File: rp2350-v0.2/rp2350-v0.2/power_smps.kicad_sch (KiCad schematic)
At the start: 23 parts, among them IC3 BQ25628ERYKR

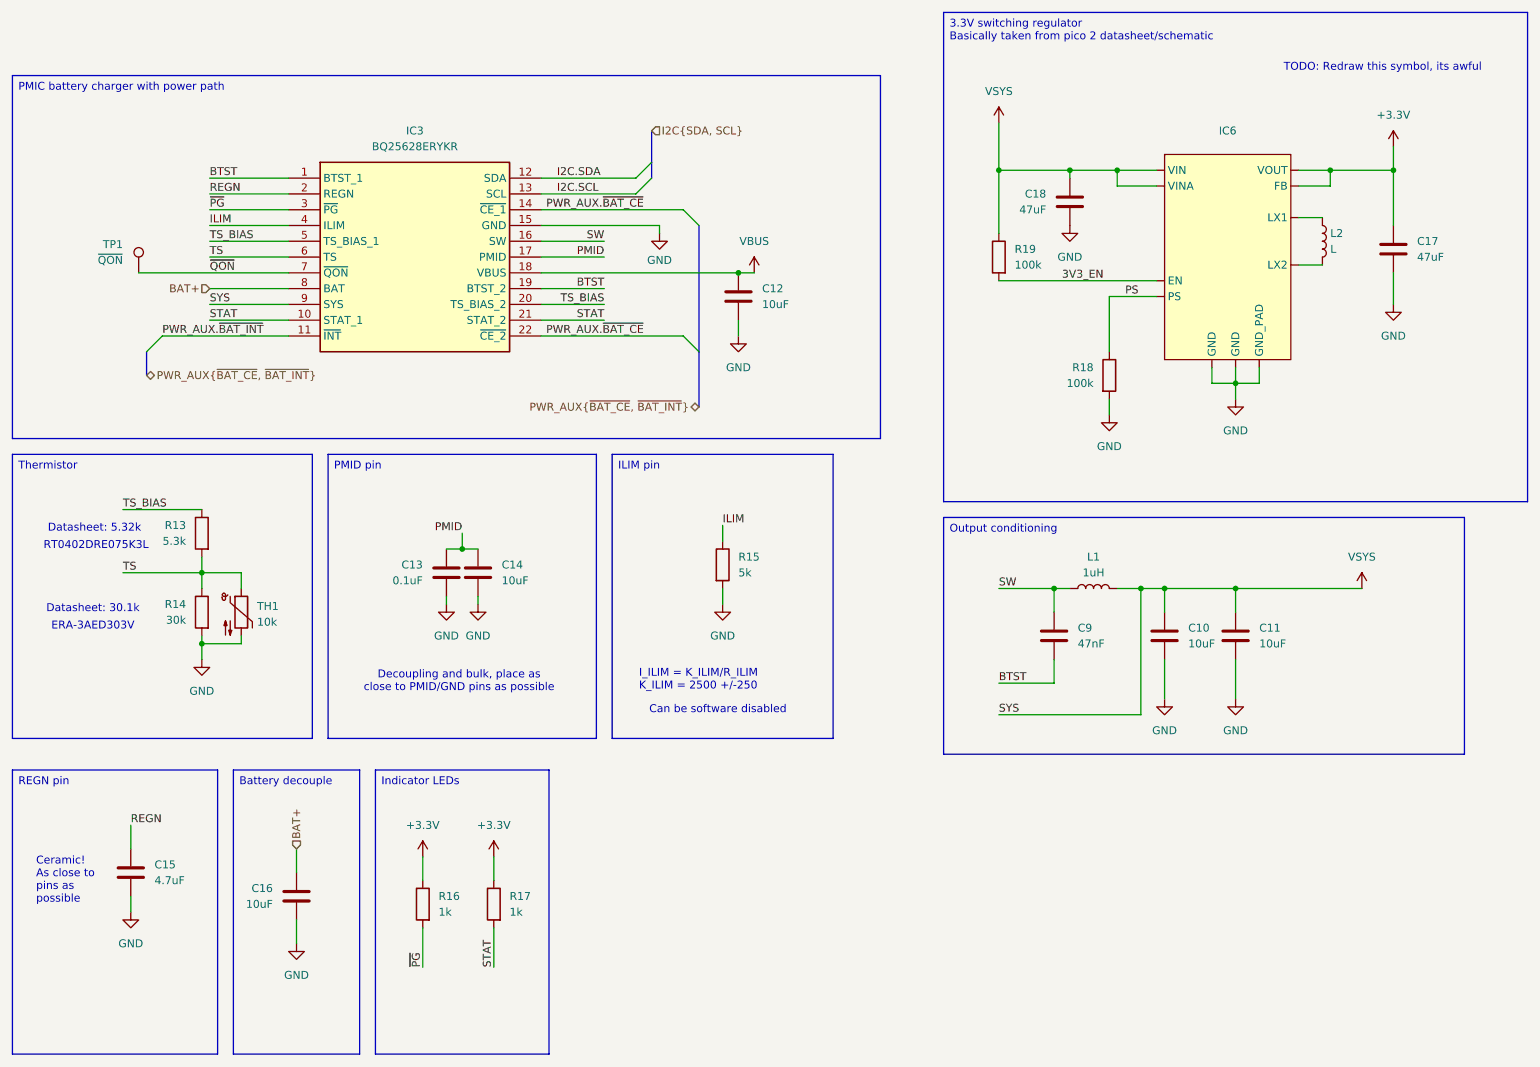
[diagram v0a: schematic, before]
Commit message: v0.2: schematic draft 1 done
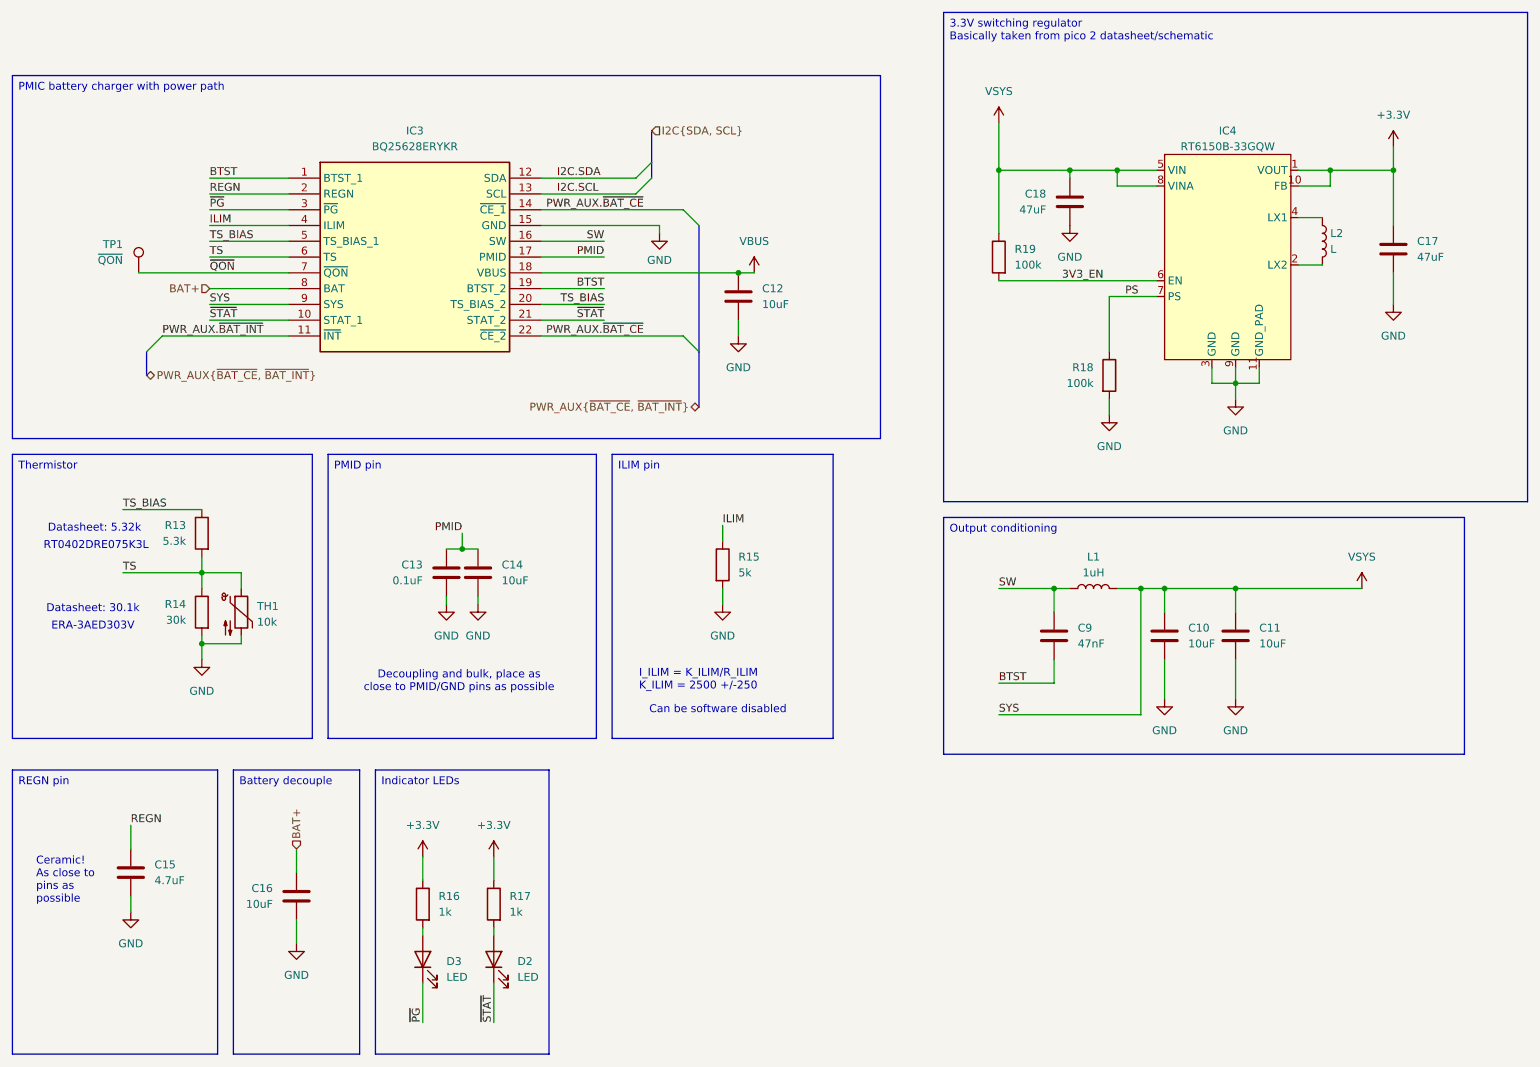
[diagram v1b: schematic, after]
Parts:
- removed IC6: ~, SamacSys_Parts:SON50P250X250X80-11N-D, symbol SamacSys_Parts:RT6150B-33GQW-Custom
- added D2, D3: LED, LED_SMD:LED_0402_1005Metric, symbol Device:LED
- added IC4: RT6150B-33GQW, SamacSys_Parts:SON50P250X250X80-11N-D, symbol CustomSymbols:RT6150B-33GQW
- TP1: footprint (none) -> TestPoint:TestPoint_Pad_2.5x2.5mm
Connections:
- net +3.3V: now also IC4.1 (VOUT), IC4.10 (FB)
- net 3V3_EN: now also IC4.6 (EN)
- net GND: now also IC4.11 (GND_PAD), IC4.3 (GND), IC4.9 (GND)
- net PS: now also IC4.7 (PS)
- net VSYS: now also IC4.5 (VIN), IC4.8 (VINA)
- net ~{PG}: now also D3.1 (K); no longer R16.2
- net at L2.1: now also IC4.4 (LX1)
- net at L2.2: now also IC4.2 (LX2)
- net STAT renamed ~{STAT}
- net ~{STAT}: now also D2.1 (K); no longer R17.2
- new net: D2.2 (A), R17.2
- new net: D3.2 (A), R16.2
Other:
- note removed: "TODO: Redraw this symbol, its awful"
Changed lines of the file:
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@@
 		)
 	)
-	(text "TODO: Redraw this symbol, its awful"
-		(exclude_from_sim no)
-		(at 259.334 25.4 0)
-		(effects
-			(font
-				(size 1.27 1.27)
-			)
-			(justify right)
-		)
-	)
 	(text_box "3.3V switching regulator\nBasically taken from pico 2 datasheet/schematic"
 		(exclude_from_sim no)
@@
 	(wire
 		(pts
-			(xy 88.9 163.83) (xy 88.9 170.18)
+			(xy 88.9 163.83) (xy 88.9 165.1)
 		)
 		(stroke
@@
 	(wire
 		(pts
-			(xy 100.33 163.83) (xy 100.33 170.18)
+			(xy 100.33 163.83) (xy 100.33 165.1)
 		)
 		(stroke
@@
 	(wire
 		(pts
+			(xy 88.9 172.72) (xy 88.9 179.07)
+		)
+		(stroke
+			(width 0)
+			(type default)
+		)
+	)
+	(wire
+		(pts
 			(xy 234.95 41.91) (xy 245.11 41.91)
 		)
@@
 	(wire
 		(pts
+			(xy 100.33 172.72) (xy 100.33 179.07)
+		)
+		(stroke
+			(width 0)
+			(type default)
+		)
+	)
+	(wire
+		(pts
 			(xy 107.95 63.5) (xy 118.11 63.5)
 		)
@@
 		)
 	)
-	(label "STAT"
+	(label "~{STAT}"
 		(at 54.61 66.04 0)
 		(effects
@@
 	)
 	(label "~{PG}"
-		(at 88.9 170.18 90)
+		(at 88.9 179.07 90)
 		(effects
 			(font
@@
 		)
 	)
-	(label "STAT"
+	(label "~{STAT}"
 		(at 118.11 66.04 180)
 		(effects
@@
 		)
 	)
-	(label "STAT"
-		(at 100.33 170.18 90)
+	(label "~{STAT}"
+		(at 100.33 179.07 90)
 		(effects
 			(font
@@
 			)
 		)
-		(property "Footprint" ""
+		(property "Footprint" "TestPoint:TestPoint_Pad_2.5x2.5mm"
 			(at 48.26 58.42 0)
 			(effects
@@
 	)
 	(symbol
-		(lib_id "SamacSys_Parts:RT6150B-33GQW-Custom")
-		(at 218.44 38.1 0)
-		(unit 1)
-		(exclude_from_sim no)
-		(in_bom yes)
-		(on_board yes)
-		(dnp no)
-		(fields_autoplaced yes)
-		(property "Reference" "IC6"
-			(at 218.44 35.56 0)
-			(effects
-				(font
-					(size 1.27 1.27)
-				)
-			)
-		)
-		(property "Value" "~"
-			(at 218.44 38.1 0)
-			(effects
-				(font
-					(size 1.27 1.27)
-				)
-			)
-		)
-		(property "Footprint" "SamacSys_Parts:SON50P250X250X80-11N-D"
-			(at 218.44 38.1 0)
-			(effects
-				(font
-					(size 1.27 1.27)
-				)
-				(hide yes)
-			)
-		)
-		(property "Datasheet" ""
-			(at 218.44 38.1 0)
-			(effects
-				(font
-					(size 1.27 1.27)
-				)
-				(hide yes)
-			)
-		)
-		(property "Description" ""
-			(at 218.44 38.1 0)
-			(effects
-				(font
-					(size 1.27 1.27)
-				)
-				(hide yes)
-			)
-		)
-		(pin ""
-		)
-		(pin ""
-		)
-		(pin ""
-		)
-		(pin ""
-		)
-		(pin ""
-		)
-		(pin ""
-		)
-		(pin ""
-		)
-		(pin ""
-		)
-		(pin ""
-		)
-		(pin ""
-		)
-		(pin ""
-		)
-		(instances
-			(project ""
-				(path "/5cbb45d4-7f83-48dd-a53b-5c75c7d1d827/e9800bf9-b30f-4ca1-94ae-2aa68cc9dec4"
-					(reference "IC6")
-					(unit 1)
-				)
-			)
-		)
-	)
-	(symbol
 		(lib_id "power:GND")
 		(at 68.58 166.37 0)
@@
 	)
 	(symbol
+		(lib_id "Device:LED")
+		(at 100.33 168.91 90)
+		(unit 1)
+		(exclude_from_sim no)
+		(in_bom yes)
+		(on_board yes)
+		(dnp no)
+		(fields_autoplaced yes)
+		(property "Reference" "D2"
+			(at 104.14 169.2274 90)
+			(effects
+				(font
+					(size 1.27 1.27)
+				)
+				(justify right)
+			)
+		)
+		(property "Value" "LED"
+			(at 104.14 171.7674 90)
+			(effects
+				(font
+					(size 1.27 1.27)
+				)
+				(justify right)
+			)
+		)
+		(property "Footprint" "LED_SMD:LED_0402_1005Metric"
+			(at 100.33 168.91 0)
+			(effects
+				(font
+					(size 1.27 1.27)
+				)
+				(hide yes)
+			)
+		)
+		(property "Datasheet" "~"
+			(at 100.33 168.91 0)
+			(effects
+				(font
+					(size 1.27 1.27)
+				)
+				(hide yes)
+			)
+		)
+		(property "Description" "Light emitting diode"
+			(at 100.33 168.91 0)
+			(effects
+				(font
+					(size 1.27 1.27)
+				)
+				(hide yes)
+			)
+		)
+		(property "Sim.Pins" "1=K 2=A"
+			(at 100.33 168.91 0)
+			(effects
+				(font
+					(size 1.27 1.27)
+				)
+				(hide yes)
+			)
+		)
+		(pin "2"
+		)
+		(pin "1"
+		)
+		(instances
+			(project ""
+				(path "/5cbb45d4-7f83-48dd-a53b-5c75c7d1d827/e9800bf9-b30f-4ca1-94ae-2aa68cc9dec4"
+					(reference "D2")
+					(unit 1)
+				)
+			)
+		)
+	)
+	(symbol
 		(lib_id "Device:C")
 		(at 97.79 106.68 0)
@@
 	)
 	(symbol
+		(lib_id "CustomSymbols:RT6150B-33GQW")
+		(at 218.44 38.1 0)
+		(unit 1)
+		(exclude_from_sim no)
+		(in_bom yes)
+		(on_board yes)
+		(dnp no)
+		(fields_autoplaced yes)
+		(property "Reference" "IC4"
+			(at 218.44 35.56 0)
+			(effects
+				(font
+					(size 1.27 1.27)
+				)
+			)
+		)
+		(property "Value" "RT6150B-33GQW"
+			(at 218.44 38.1 0)
+			(effects
+				(font
+					(size 1.27 1.27)
+				)
+			)
+		)
+		(property "Footprint" "SamacSys_Parts:SON50P250X250X80-11N-D"
+			(at 218.44 38.1 0)
+			(effects
+				(font
+					(size 1.27 1.27)
+				)
+				(hide yes)
+			)
+		)
+		(property "Datasheet" ""
+			(at 218.44 38.1 0)
+			(effects
+				(font
+					(size 1.27 1.27)
+				)
+				(hide yes)
+			)
+		)
+		(property "Description" ""
+			(at 218.44 38.1 0)
+			(effects
+				(font
+					(size 1.27 1.27)
+				)
+				(hide yes)
+			)
+		)
+		(pin "4"
+		)
+		(pin "1"
+		)
+		(pin "6"
+		)
+		(pin "11"
+		)
+		(pin "8"
+		)
+		(pin "10"
+		)
+		(pin "3"
+		)
+		(pin "5"
+		)
+		(pin "7"
+		)
+		(pin "9"
+		)
+		(pin "2"
+		)
+		(instances
+			(project ""
+				(path "/5cbb45d4-7f83-48dd-a53b-5c75c7d1d827/e9800bf9-b30f-4ca1-94ae-2aa68cc9dec4"
+					(reference "IC4")
+					(unit 1)
+				)
+			)
+		)
+	)
+	(symbol
 		(lib_id "Device:C")
 		(at 219.71 116.84 0)
@@
 					(unit 1)
 				)
+			)
+		)
+	)
+	(symbol
+		(lib_id "Device:LED")
+		(at 88.9 168.91 90)
+		(unit 1)
+		(exclude_from_sim no)
+		(in_bom yes)
+		(on_board yes)
+		(dnp no)
+		(fields_autoplaced yes)
+		(property "Reference" "D3"
+			(at 92.71 169.2274 90)
+			(effects
+				(font
+					(size 1.27 1.27)
+				)
+				(justify right)
+			)
+		)
+		(property "Value" "LED"
+			(at 92.71 171.7674 90)
+			(effects
+				(font
+					(size 1.27 1.27)
+				)
+				(justify right)
+			)
+		)
+		(property "Footprint" "LED_SMD:LED_0402_1005Metric"
+			(at 88.9 168.91 0)
+			(effects
+				(font
+					(size 1.27 1.27)
+				)
+				(hide yes)
+			)
+		)
+		(property "Datasheet" "~"
+			(at 88.9 168.91 0)
+			(effects
+				(font
+					(size 1.27 1.27)
+				)
+				(hide yes)
+			)
+		)
+		(property "Description" "Light emitting diode"
+			(at 88.9 168.91 0)
+			(effects
+				(font
+					(size 1.27 1.27)
+				)
+				(hide yes)
+			)
+		)
+		(property "Sim.Pins" "1=K 2=A"
+			(at 88.9 168.91 0)
+			(effects
+				(font
+					(size 1.27 1.27)
+				)
+				(hide yes)
+			)
+		)
+		(pin "2"
+		)
+		(pin "1"
+		)
+		(instances
+			(project "rp2350-v0.2"
+				(path "/5cbb45d4-7f83-48dd-a53b-5c75c7d1d827/e9800bf9-b30f-4ca1-94ae-2aa68cc9dec4"
+					(reference "D3")
+					(unit 1)
+				)

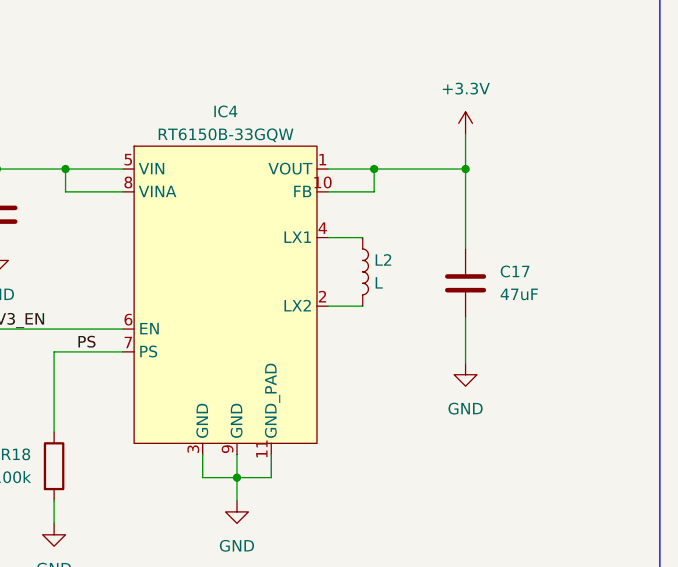
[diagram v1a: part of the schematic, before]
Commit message: v0.2: final big checks done, fixed IrDA footprint
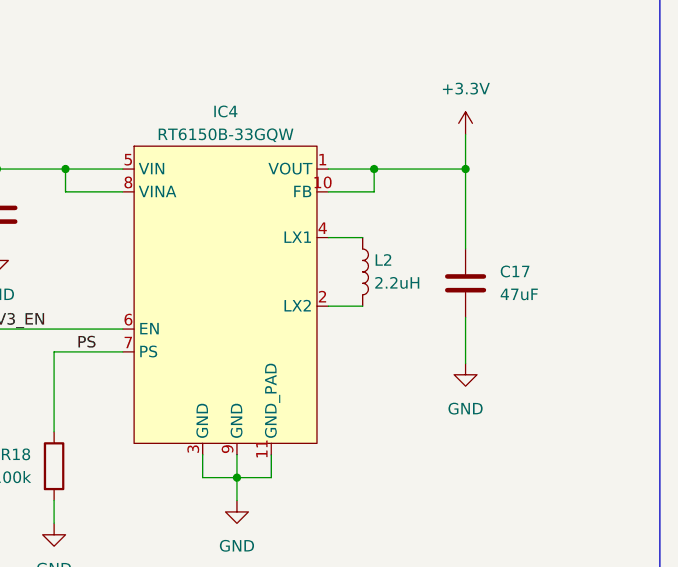
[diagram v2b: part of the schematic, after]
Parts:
- L2: value L -> 2.2uH
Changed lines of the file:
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@@
 			)
 		)
-		(property "Value" "L"
+		(property "Value" "2.2uH"
 			(at 234.95 54.6099 0)
 			(effects

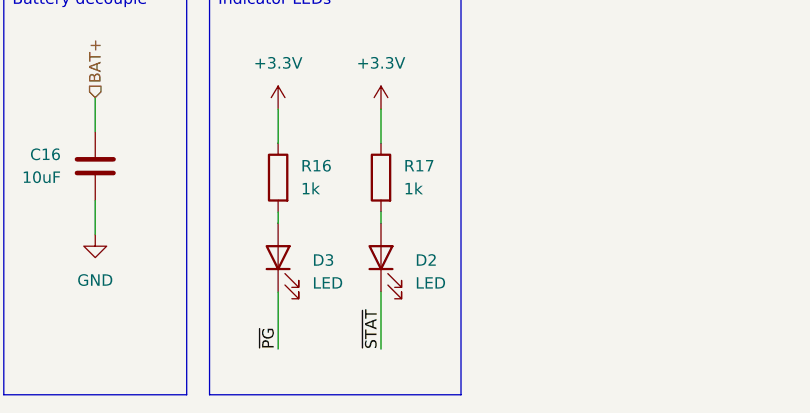
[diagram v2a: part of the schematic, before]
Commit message: v0.2: update battery connector and labels
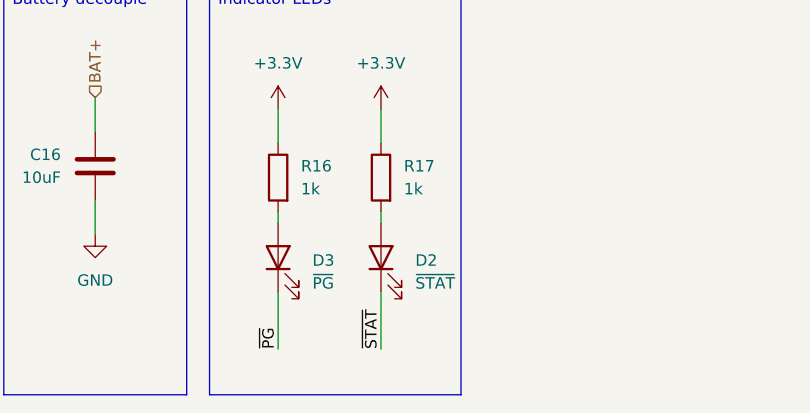
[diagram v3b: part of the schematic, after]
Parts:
- D2: value LED -> ~{STAT}
- D3: value LED -> ~{PG}
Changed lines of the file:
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@@
 			)
 		)
-		(property "Value" "LED"
+		(property "Value" "~{STAT}"
 			(at 104.14 171.7674 90)
 			(effects
@@
 			)
 		)
-		(property "Value" "LED"
+		(property "Value" "~{PG}"
 			(at 92.71 171.7674 90)
 			(effects
